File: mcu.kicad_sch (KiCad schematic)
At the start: 44 parts, among them J1 1156915, J6 Conn_02x05_Odd_Even, J7 Conn_01x05_Pin, U7 REF3033, U8 STM32F407VGTx, Y1 8MHz

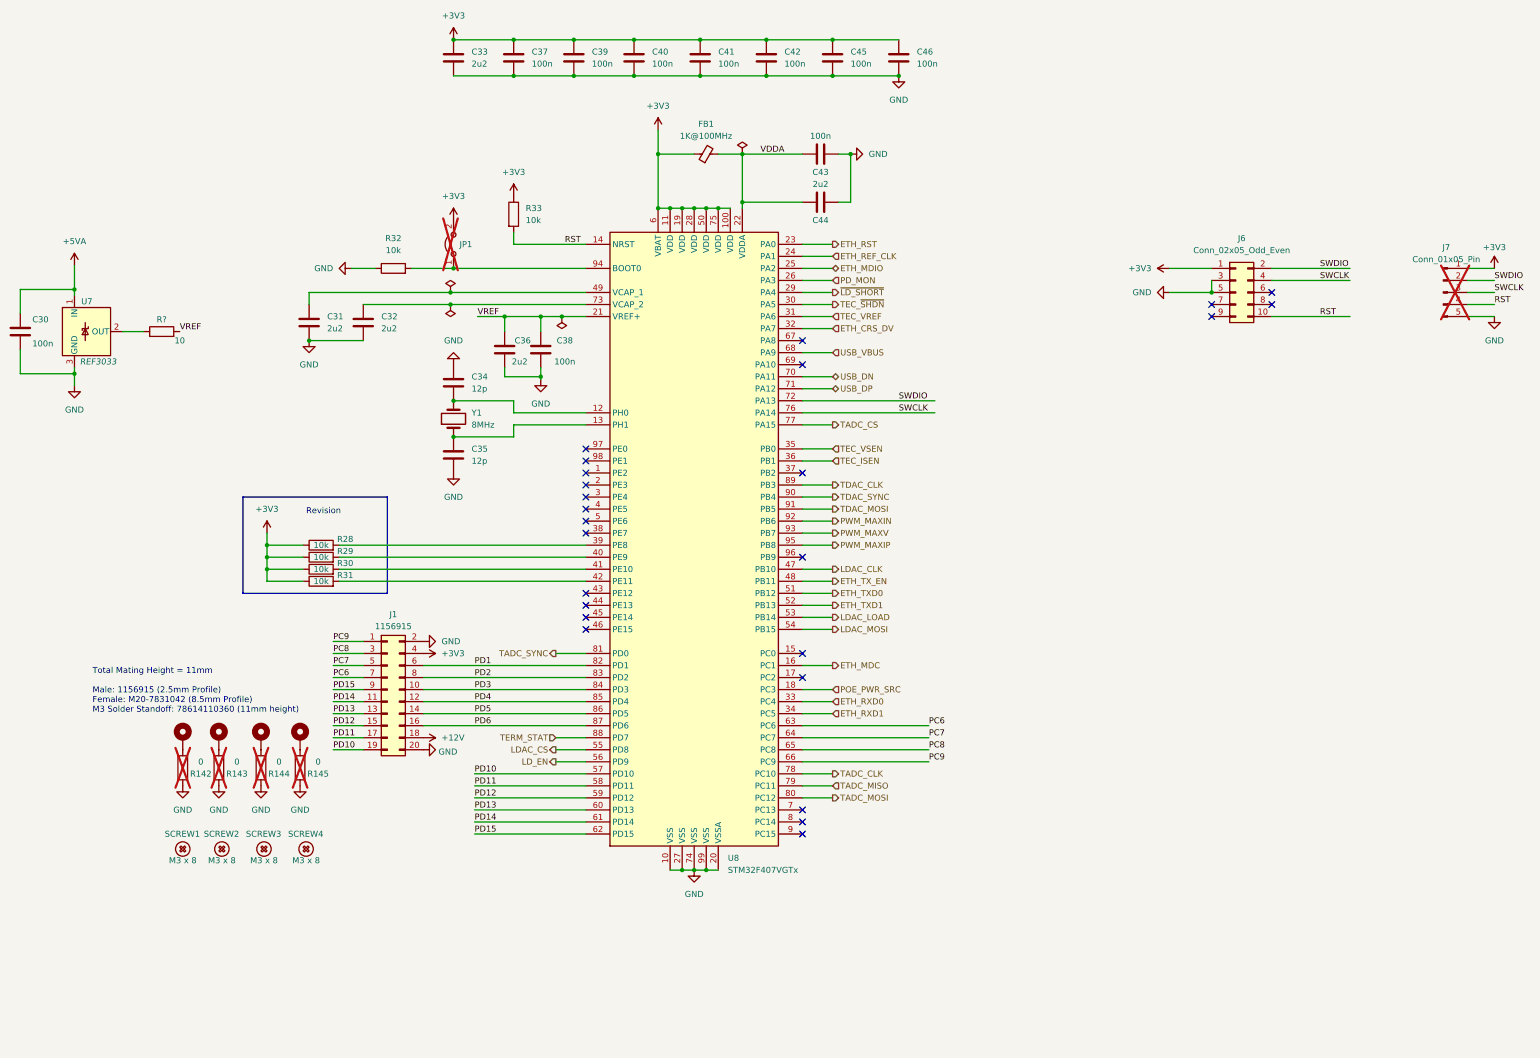
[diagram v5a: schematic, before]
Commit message: Reassign Reference Designators for all Symbols
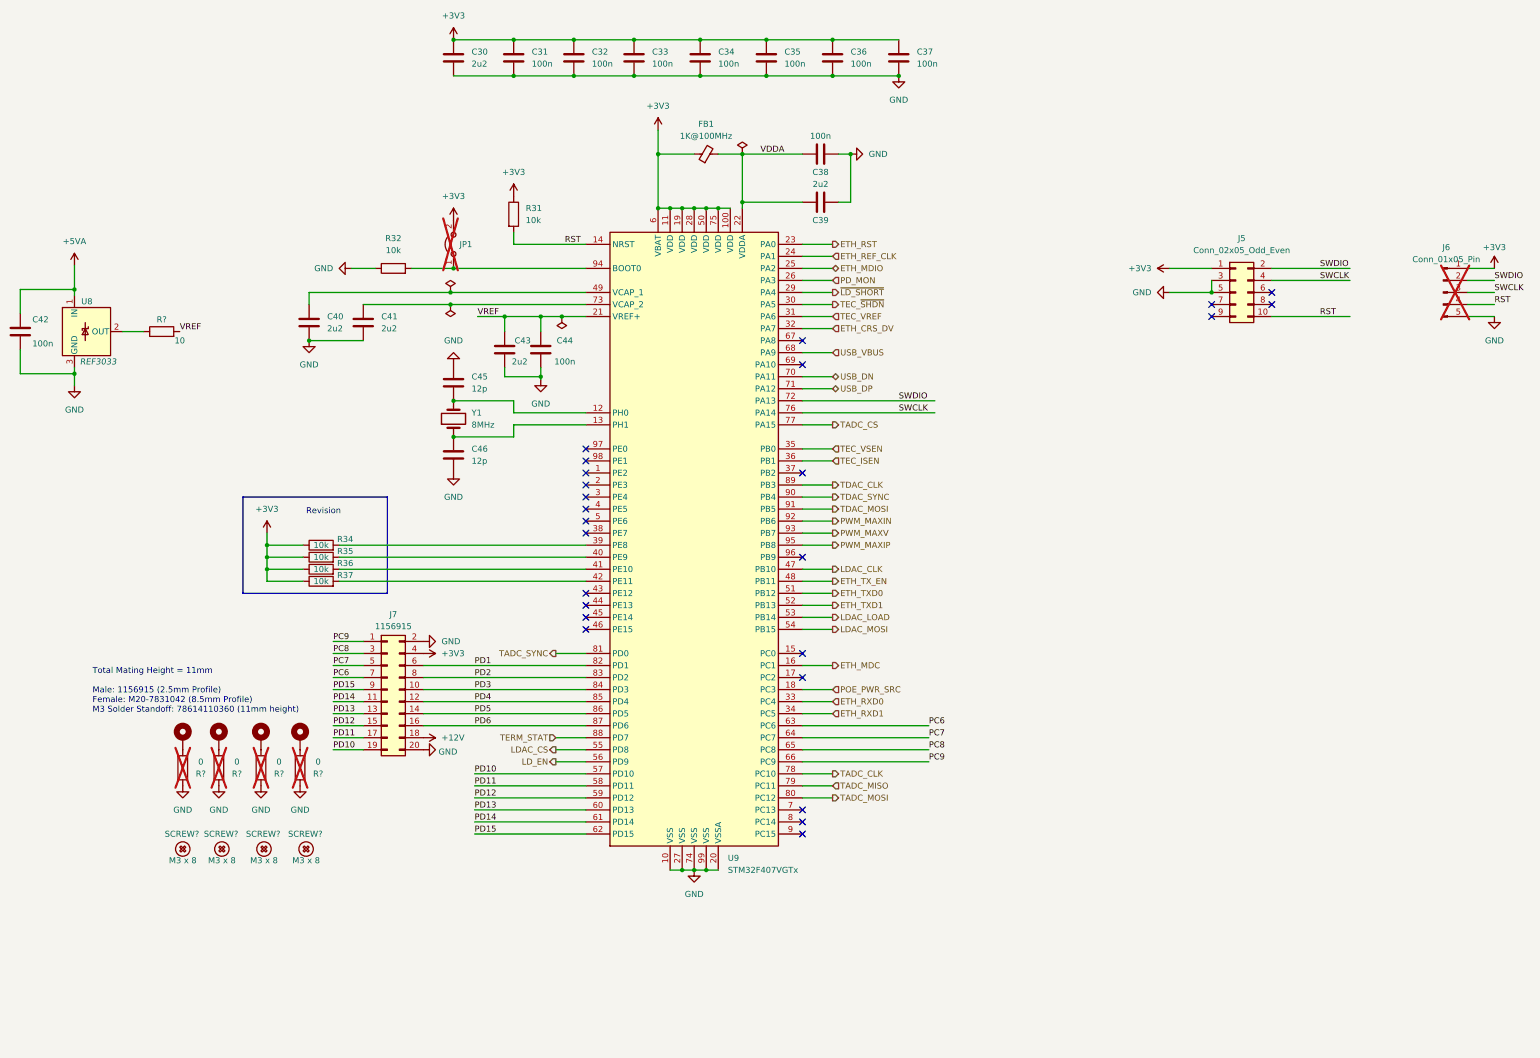
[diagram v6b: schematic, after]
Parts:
- renumbered C33 to C30, C37 to C31, C39 to C32, C40 to C33, C41 to C34, C42 to C35, C45 to C36, C46 to C37, C43 to C38, C44 to C39, C31 to C40, C32 to C41, C30 to C42, C36 to C43, C38 to C44, C34 to C45, C35 to C46, H6 to H?, H5 to H?, H7 to H?, H8 to H?, J6 to J5, J7 to J6, J1 to J7, R33 to R31, R28 to R34, R29 to R35, R30 to R36, R31 to R37, R143 to R?, R142 to R?, R144 to R?, R145 to R?, SCREW2 to SCREW?, SCREW1 to SCREW?, SCREW4 to SCREW?, SCREW3 to SCREW?, U7 to U8, U8 to U9

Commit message: sch: Not to include TPs in BOM. Add prod comments - LTC6655 Vref adds production comments
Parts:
- H?: MFR_PN_ALT (none) -> 9774110360R; MFT_PN_ALT 9774110360R -> (none)
- J5: Comment (none) -> Manufacturer: Adafruit
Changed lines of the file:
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@@
+      (effects (font (size 1.27 1.27)) hide)
+    )
+    (property "Comment" "Manufacturer: Adafruit" (at 317.5 91.44 0)
       (effects (font (size 1.27 1.27)) hide)
     )
@@
       (effects (font (size 1.27 1.27)) hide)
     )
-    (property "MFT_PN_ALT" "9774110360R" (at 111.76 185.42 0)
-      (effects (font (size 1.27 1.27)) hide)
-    )
+    (property "MFR_PN_ALT" "9774110360R" (at 111.76 185.42 0)
+      (effects (font (size 1.27 1.27)) hide)
+    )

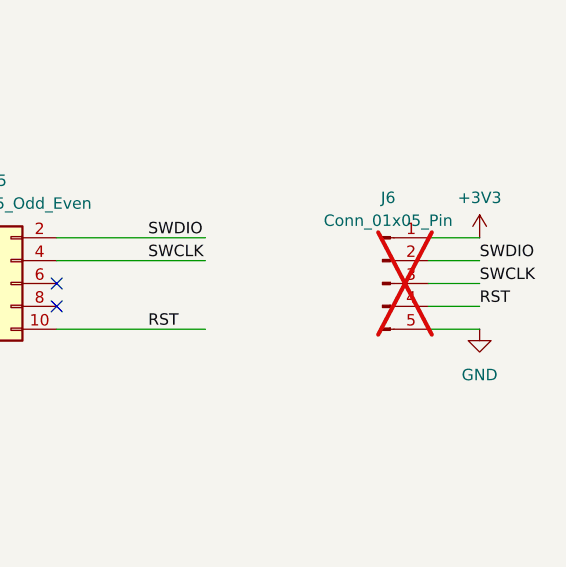
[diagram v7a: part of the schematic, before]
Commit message: sch: Set the mcu 2.54mm Prog HDR to be placed
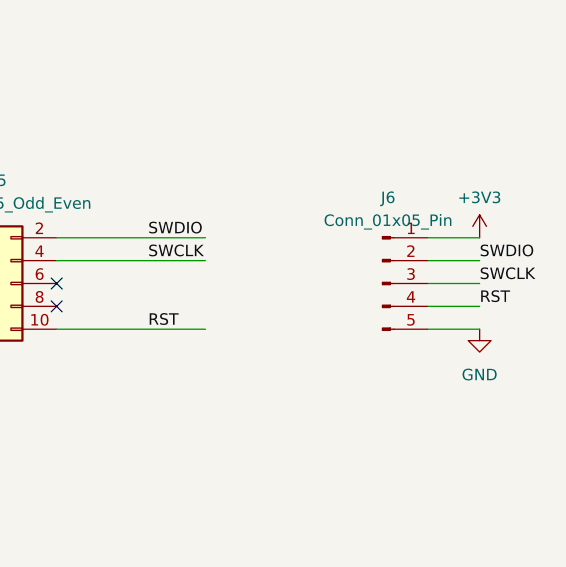
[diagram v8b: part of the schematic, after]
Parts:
- J6: Comment (none) -> Generic 2.54mm x 5 Pin Header; MFR_PN (none) -> HB-PH3-25415PB2GOP; now fitted
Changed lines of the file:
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@@
   )
   (symbol (lib_id "Connector:Conn_01x05_Pin") (at 361.315 91.44 0) (unit 1)
-    (in_bom yes) (on_board yes) (dnp yes) (fields_autoplaced)
+    (in_bom yes) (on_board yes) (dnp no) (fields_autoplaced)
     (property "Reference" "J6" (at 361.95 81.915 0)
       (effects (font (size 1.27 1.27)))
@@
       (effects (font (size 1.27 1.27)) hide)
     )
+    (property "MFR_PN" "HB-PH3-25415PB2GOP" (at 361.315 91.44 0)
+      (effects (font (size 1.27 1.27)) hide)
+    )
+    (property "Comment" "Generic 2.54mm x 5 Pin Header" (at 361.315 91.44 0)
+      (effects (font (size 1.27 1.27)) hide)
+    )
